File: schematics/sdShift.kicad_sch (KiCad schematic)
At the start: 3 parts, among them J20 port

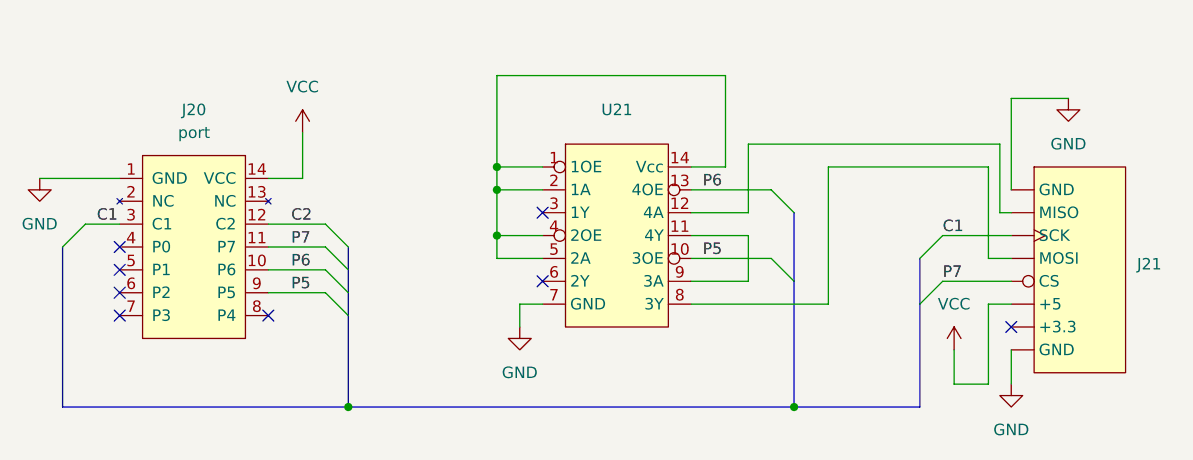
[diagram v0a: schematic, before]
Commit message: Fix errors in schematics
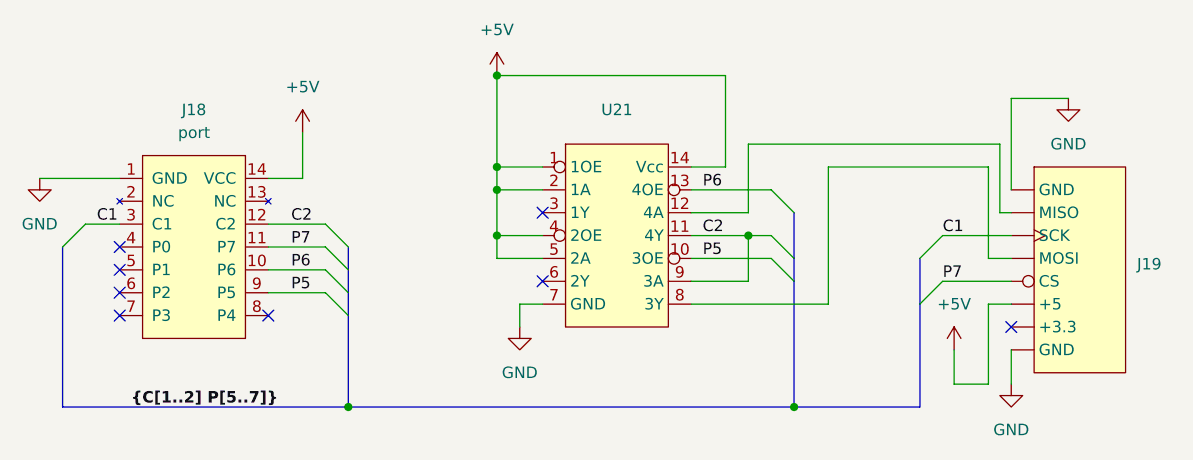
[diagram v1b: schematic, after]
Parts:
- removed J21: ~, symbol 6502:SD_adapter
- added J19: ~, symbol 6502:SDconnector
- renumbered J20 to J18
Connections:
- net VCC is gone; now on net +5V: J18.14 (VCC)
- net C1: now also J19. (SCK)
- net C2: now also U21.11 (4Y), U21.9 (3A)
- net GND: now also J19. (SCK)
- net P7: now also J19. (SCK)
- net at U21.12 (4A): now also J19. (SCK)
- net at U21.8 (3Y): now also J19. (SCK)
- net +5V: now reaches U21.1 (1OE), U21.14 (Vcc), U21.2 (1A), U21.4 (2OE), U21.5 (2A)
- net +5V: now also J19. (SCK)

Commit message: Update sd adapter schematic
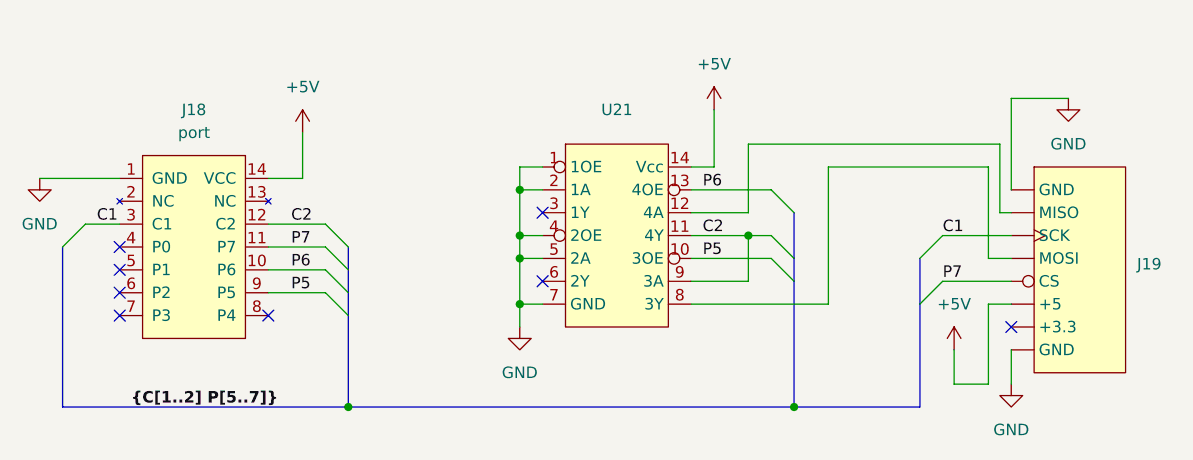
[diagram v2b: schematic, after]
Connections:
- net +5V: no longer U21.1 (1OE), U21.2 (1A), U21.4 (2OE), U21.5 (2A)
- net GND: now also U21.1 (1OE), U21.2 (1A), U21.4 (2OE), U21.5 (2A)
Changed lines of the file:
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@@
 	)
 	(junction
-		(at 104.14 66.04)
+		(at 106.68 83.82)
 		(diameter 0)
 		(color 0 0 0 0)
@@
 	)
 	(junction
+		(at 106.68 91.44)
+		(diameter 0)
+		(color 0 0 0 0)
+	)
+	(junction
+		(at 106.68 78.74)
+		(diameter 0)
+		(color 0 0 0 0)
+	)
+	(junction
 		(at 132.08 83.82)
 		(diameter 0)
@@
 	)
 	(junction
-		(at 104.14 76.2)
-		(diameter 0)
-		(color 0 0 0 0)
-	)
-	(junction
-		(at 104.14 78.74)
-		(diameter 0)
-		(color 0 0 0 0)
-	)
-	(junction
-		(at 104.14 83.82)
+		(at 106.68 86.36)
 		(diameter 0)
 		(color 0 0 0 0)
@@
 	(wire
 		(pts
-			(xy 104.14 66.04) (xy 104.14 76.2)
-		)
-		(stroke
-			(width 0)
-			(type default)
-		)
-	)
-	(wire
-		(pts
 			(xy 140.97 91.44) (xy 140.97 76.2)
 		)
@@
 		)
 	)
+	(wire
+		(pts
+			(xy 106.68 86.36) (xy 109.22 86.36)
+		)
+		(stroke
+			(width 0)
+			(type default)
+		)
+	)
+	(wire
+		(pts
+			(xy 106.68 78.74) (xy 106.68 83.82)
+		)
+		(stroke
+			(width 0)
+			(type default)
+		)
+	)
 	(bus
 		(pts
@@
 		)
 	)
-	(wire
-		(pts
-			(xy 129.54 66.04) (xy 104.14 66.04)
-		)
-		(stroke
-			(width 0)
-			(type default)
-		)
-	)
 	(bus
 		(pts
@@
 	(wire
 		(pts
+			(xy 109.22 76.2) (xy 106.68 76.2)
+		)
+		(stroke
+			(width 0)
+			(type default)
+		)
+	)
+	(wire
+		(pts
 			(xy 58.42 82.55) (xy 62.23 82.55)
 		)
@@
 	(wire
 		(pts
-			(xy 104.14 76.2) (xy 104.14 78.74)
+			(xy 106.68 78.74) (xy 109.22 78.74)
 		)
 		(stroke
@@
 		)
 	)
+	(wire
+		(pts
+			(xy 106.68 83.82) (xy 106.68 86.36)
+		)
+		(stroke
+			(width 0)
+			(type default)
+		)
+	)
 	(bus
 		(pts
@@
 	(wire
 		(pts
-			(xy 104.14 83.82) (xy 104.14 78.74)
+			(xy 106.68 83.82) (xy 109.22 83.82)
 		)
 		(stroke
@@
 	(wire
 		(pts
-			(xy 104.14 86.36) (xy 104.14 83.82)
-		)
-		(stroke
-			(width 0)
-			(type default)
-		)
-	)
-	(wire
-		(pts
 			(xy 161.29 96.52) (xy 161.29 100.33)
 		)
@@
 	(wire
 		(pts
-			(xy 129.54 76.2) (xy 129.54 66.04)
-		)
-		(stroke
-			(width 0)
-			(type default)
-		)
-	)
-	(wire
-		(pts
-			(xy 109.22 86.36) (xy 104.14 86.36)
+			(xy 128.27 76.2) (xy 128.27 69.85)
 		)
 		(stroke
@@
 	(wire
 		(pts
-			(xy 104.14 76.2) (xy 109.22 76.2)
-		)
-		(stroke
-			(width 0)
-			(type default)
-		)
-	)
-	(wire
-		(pts
 			(xy 132.08 83.82) (xy 132.08 88.9)
 		)
@@
 	(wire
 		(pts
-			(xy 104.14 78.74) (xy 109.22 78.74)
-		)
-		(stroke
-			(width 0)
-			(type default)
-		)
-	)
-	(wire
-		(pts
-			(xy 109.22 83.82) (xy 104.14 83.82)
+			(xy 106.68 86.36) (xy 106.68 91.44)
 		)
 		(stroke
@@
 	(wire
 		(pts
-			(xy 125.73 76.2) (xy 129.54 76.2)
+			(xy 125.73 76.2) (xy 128.27 76.2)
 		)
 		(stroke
@@
 		(pts
 			(xy 158.75 76.2) (xy 158.75 86.36)
+		)
+		(stroke
+			(width 0)
+			(type default)
+		)
+	)
+	(wire
+		(pts
+			(xy 106.68 76.2) (xy 106.68 78.74)
 		)
 		(stroke
@@
 	(symbol
 		(lib_id "power:+5V")
-		(at 104.14 66.04 0)
+		(at 128.27 69.85 0)
 		(unit 1)
 		(exclude_from_sim no)
@@
 		(fields_autoplaced yes)
 		(property "Reference" "#PWR091"
-			(at 104.14 69.85 0)
+			(at 128.27 73.66 0)
 			(effects
 				(font
@@
 		)
 		(property "Value" "+5V"
-			(at 104.14 60.96 0)
+			(at 128.27 64.77 0)
 			(effects
 				(font
@@
 		)
 		(property "Footprint" ""
-			(at 104.14 66.04 0)
+			(at 128.27 69.85 0)
 			(effects
 				(font
@@
 		)
 		(property "Datasheet" ""
-			(at 104.14 66.04 0)
+			(at 128.27 69.85 0)
 			(effects
 				(font
@@
 		)
 		(property "Description" "Power symbol creates a global label with name \"+5V\""
-			(at 104.14 66.04 0)
+			(at 128.27 69.85 0)
 			(effects
 				(font

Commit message: Update schematics for peripherals
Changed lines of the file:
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@@
 				)
 				(justify left)
+				(hide yes)
 			)
 		)
@@
 					(size 1.27 1.27)
 				)
-			)
-		)
+				(hide yes)
+			)
+		)

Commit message: Add resistor to clock in peripherals board
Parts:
- J19, U21: value ~ -> (none)
